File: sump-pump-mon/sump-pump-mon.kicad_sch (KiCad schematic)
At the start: 46 parts, among them J1 Main Input, J2 Wall Power, J3 Battery, J4 Display_Conn, J5 Aux Input, J6 I2C, SW1 SW_Push, SW2 SW_Push, SW3 MODE, SW4 POWER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

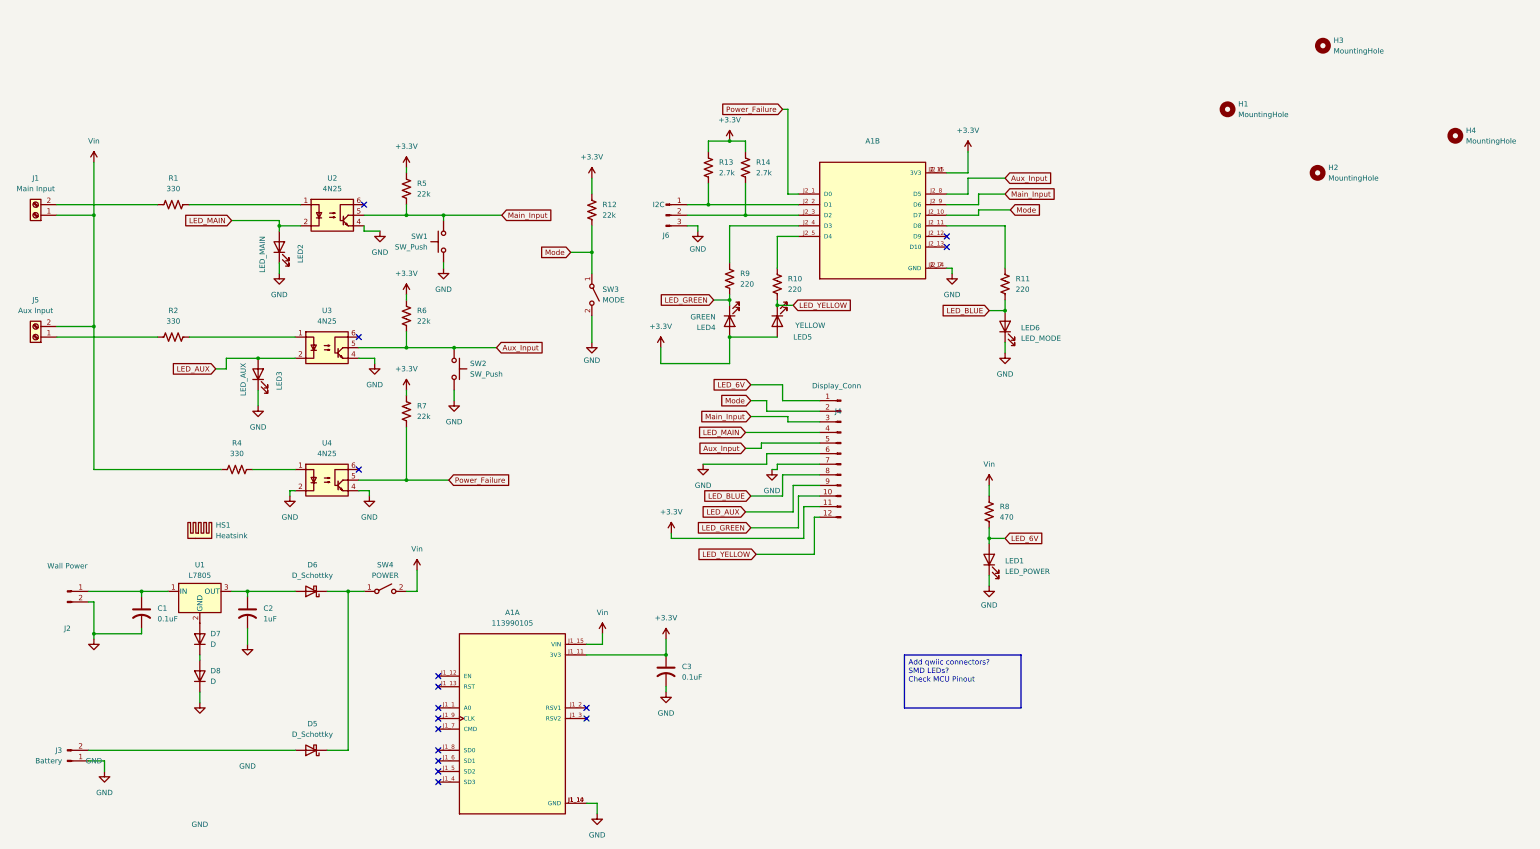
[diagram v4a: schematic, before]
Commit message: Add Stemma connectors; Add 3d models; Cleanup silk
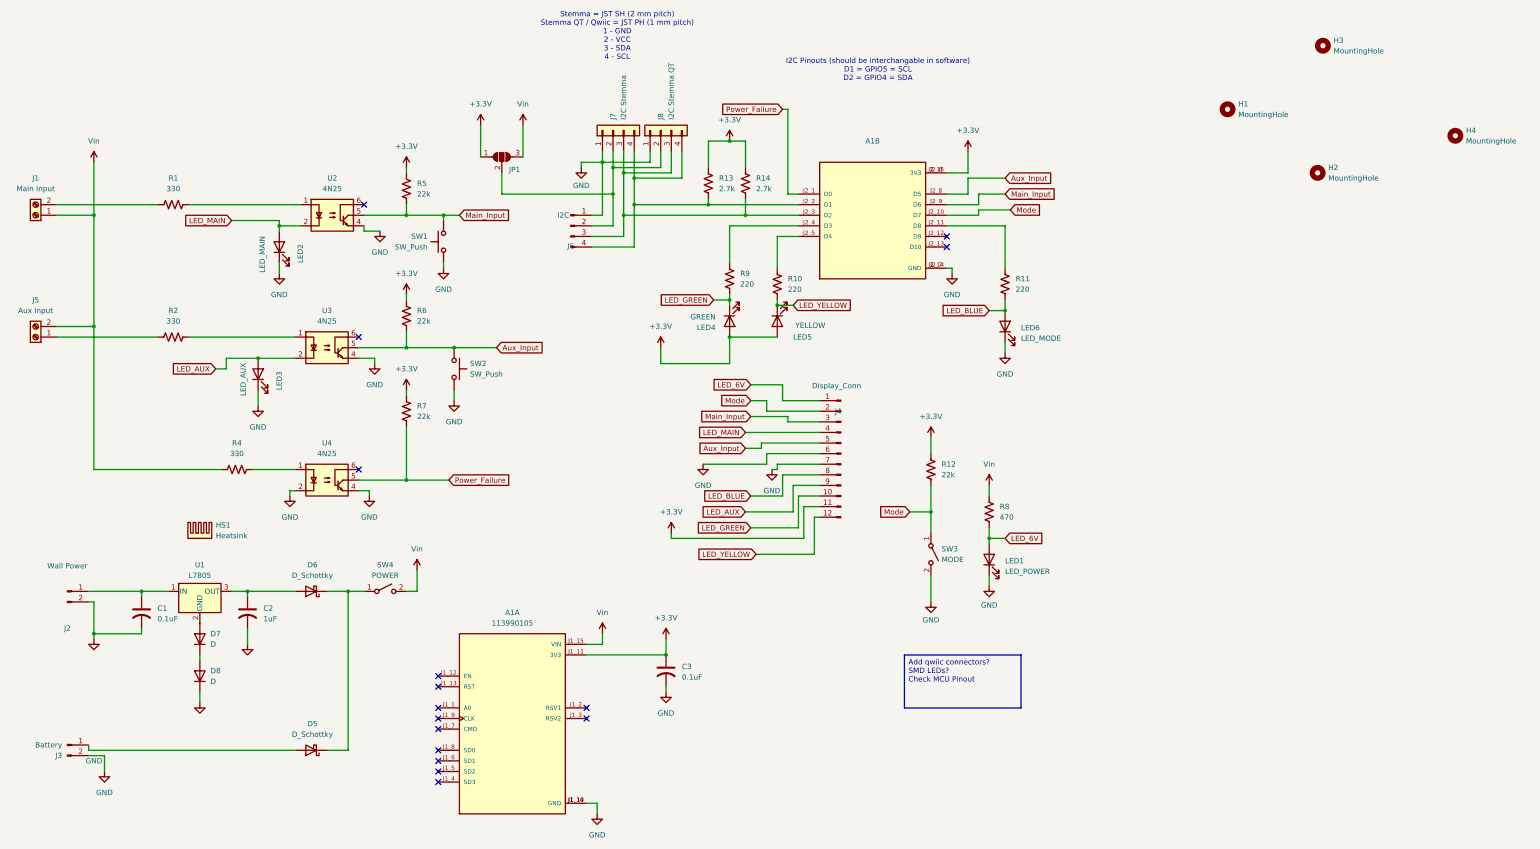
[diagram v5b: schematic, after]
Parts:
- added J7: I2C Stemma, Connector_JST:JST_PH_B4B-PH-SM4-TB_1x04-1MP_P2.00mm_Vertical, symbol Connector_Generic:Conn_01x04
- added J8: I2C Stemma QT, Connector_JST:JST_SH_SM04B-SRSS-TB_1x04-1MP_P1.00mm_Horizontal, symbol Connector_Generic:Conn_01x04
- added JP1: SolderJumper_3_Open, Jumper:SolderJumper-3_P1.3mm_Open_Pad1.0x1.5mm_NumberLabels, symbol Jumper:SolderJumper_3_Open
- J6: footprint Connector_JST:JST_XH_B3B-XH-A_1x03_P2.50mm_Vertical -> Connector_JST:JST_XH_B4B-XH-A_1x04_P2.50mm_Vertical; symbol Connector:Conn_01x03_Pin -> Connector:Conn_01x04_Pin
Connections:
- net +3.3V: now also JP1.1 (A)
- net GND: now also J3.2 (Pin_2), J6.1 (Pin_1), J7.1 (Pin_1), J8.1 (Pin_1); no longer J3.1 (Pin_1), J6.3 (Pin_3)
- net Vin: now also JP1.3 (B)
- net at D5.2 (A): now also J3.1 (Pin_1); no longer J3.2 (Pin_2)
- net at A1.J2_2 (D1), R13.2: now also J6.4 (Pin_4), J7.4 (Pin_4), J8.4 (Pin_4); no longer J6.1 (Pin_1)
- net at A1.J2_3 (D2), R14.2: now also J6.3 (Pin_3), J7.3 (Pin_3), J8.3 (Pin_3); no longer J6.2 (Pin_2)
- new net: J6.2 (Pin_2), J7.2 (Pin_2), J8.2 (Pin_2), JP1.2 (C)
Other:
- note added: "I2C Pinouts (should be interchangable in software) D1 = GPIO5 = SCL D2 = GPIO4 = SDA"
- note added: "Stemma = JST SH (2 mm pitch) Stemma QT / Qwiic = JST PH (1 mm pitch) 1 - GND 2 - VCC 3 - SDA 4 - SCL"
- moved on the sheet: J3, R12, R13, R14, SW3

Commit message: Add note about mode switch
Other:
- note added: "IS MODE SWITCH RIGHT? DOES IT NEED TO GO TO 2 CONNECTORS???"
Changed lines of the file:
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@@
 		(rev "1.0")
+	)
+	(text "IS MODE SWITCH RIGHT?\nDOES IT NEED TO GO TO 2 CONNECTORS???"
+		(exclude_from_sim no)
+		(at 324.358 127.508 0)
+		(effects
+			(font
+				(size 2.54 2.54)
+				(thickness 0.254)
+				(bold yes)
+				(color 255 0 13 1)
+			)
+		)
 	)
 	(text "Stemma = JST SH (2 mm pitch)\nStemma QT / Qwiic = JST PH (1 mm pitch)\n1 - GND\n2 - VCC\n3 - SDA\n4 - SCL\n"

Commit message: updated silkscreen & renamed nets
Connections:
- net Aux_Input renamed Yellow_Button
- net Main_Input renamed Green_Button
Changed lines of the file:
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@@
 		)
 	)
-	(global_label "Aux_Input"
+	(global_label "Yellow_Button"
 		(shape input)
 		(at 130.81 72.39 0)
@@
 		)
 	)
-	(global_label "Aux_Input"
+	(global_label "Yellow_Button"
 		(shape input)
 		(at 252.73 31.75 0)
@@
 		)
 	)
-	(global_label "Aux_Input"
+	(global_label "Yellow_Button"
 		(shape input)
 		(at 190.5 96.52 180)
@@
 		)
 	)
-	(global_label "Main_Input"
+	(global_label "Green_Button"
 		(shape input)
 		(at 252.73 35.56 0)
@@
 		)
 	)
-	(global_label "Main_Input"
+	(global_label "Green_Button"
 		(shape input)
 		(at 191.77 88.9 180)
@@
 		)
 	)
-	(global_label "Main_Input"
+	(global_label "Green_Button"
 		(shape input)
 		(at 121.92 40.64 0)

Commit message: Delete notes
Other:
- note removed: "IS MODE SWITCH RIGHT? DOES IT NEED TO GO TO 2 CONNECTORS???"
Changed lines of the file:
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@@
 		(rev "1.0")
-	)
-	(text "IS MODE SWITCH RIGHT?\nDOES IT NEED TO GO TO 2 CONNECTORS???"
-		(exclude_from_sim no)
-		(at 324.358 127.508 0)
-		(effects
-			(font
-				(size 2.54 2.54)
-				(thickness 0.254)
-				(bold yes)
-				(color 255 0 13 1)
-			)
-		)
 	)
 	(text "Stemma = JST SH (2 mm pitch)\nStemma QT / Qwiic = JST PH (1 mm pitch)\n1 - GND\n2 - VCC\n3 - SDA\n4 - SCL\n"
@@
 		)
 	)
-	(text_box "Add qwiic connectors?\nSMD LEDs?\nCheck MCU Pinout"
+	(text_box "SMD LEDs?\n"
 		(exclude_from_sim no)
 		(at 228.6 146.05 0)
